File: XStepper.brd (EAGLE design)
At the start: 100.3 x 80 mm, 75 parts, among them IC2 7812TV, Q2 16 MHZ

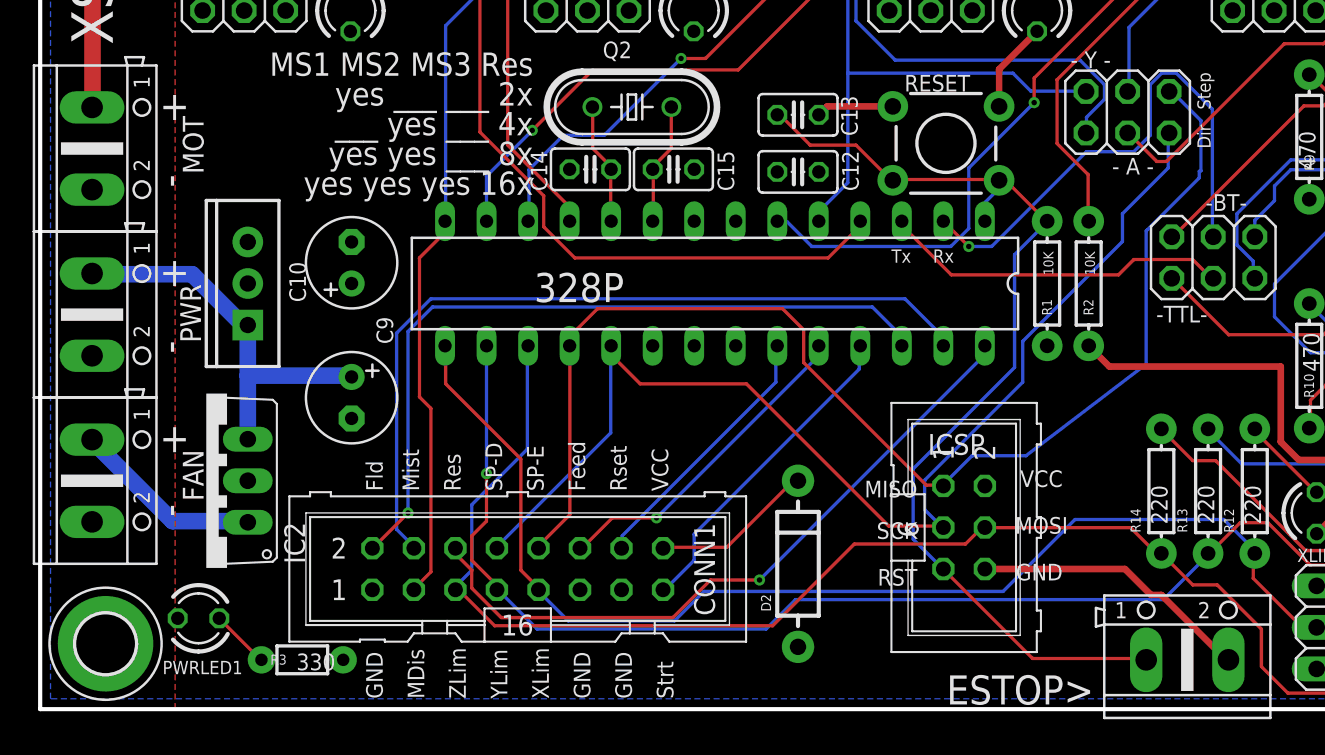
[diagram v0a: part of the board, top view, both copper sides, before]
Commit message: - add 7812 regulator for fan and main 5V voltage regulator
- change c10 to small cap cuz he get only 12v with new regulator
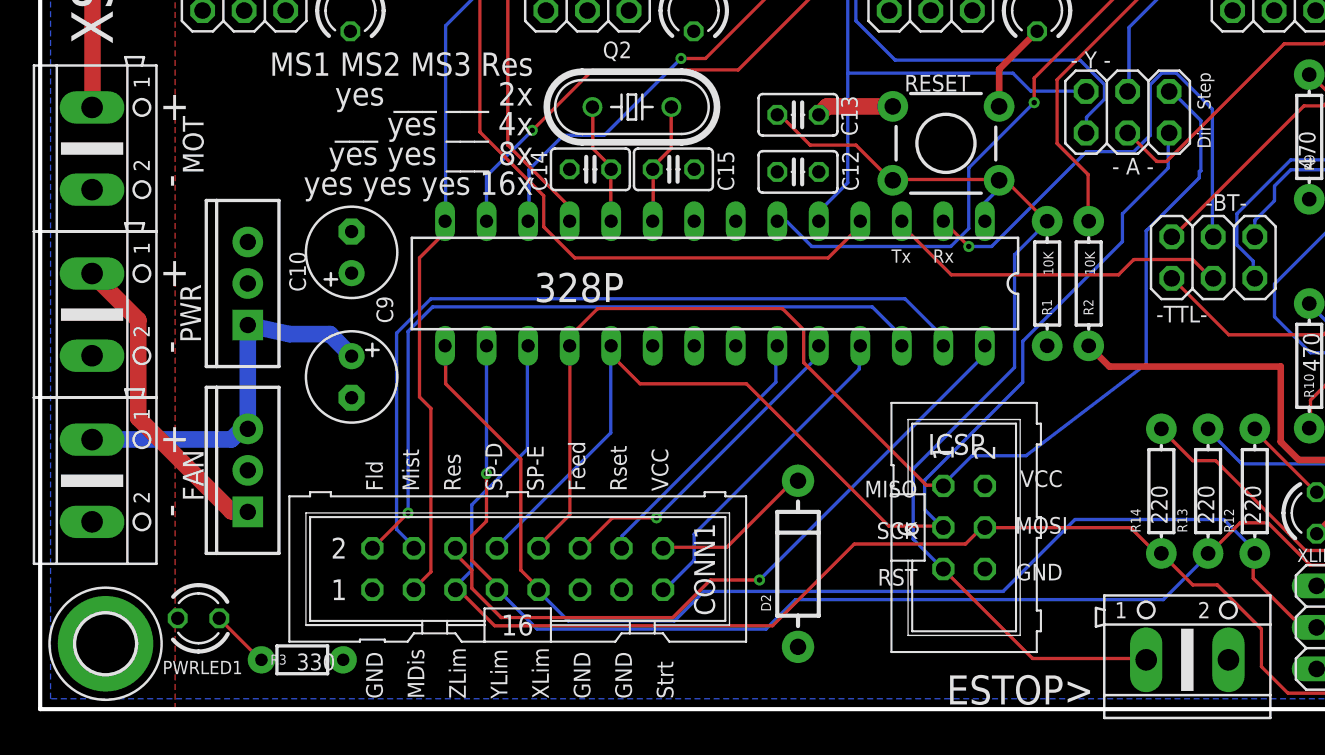
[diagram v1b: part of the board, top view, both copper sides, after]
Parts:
- removed IC2: 7812TV, linear:TO220V
- added 7812: (no value), SparkFun-PowerIC:TO220-IGO
- moved C9 1.27 mm to (19.1, 20.3)
- moved C10 0.64 mm to (19.1, 27.9)
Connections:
- removed net N$46: FAN.1, IC2.1
- new net +24V: 7812.IN, PWR.1
- net 12V: now also 7812.OUT, FAN.1; no longer IC2.3, PWR.1
- net GND: now also 7812.GND; no longer IC2.2
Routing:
- net +24V: track 0.00 -> 19.1 mm
- net GND: track 53.6 -> 36.8 mm
- net N$46: track 11.7 -> 0.00 mm
- net 12V: track 24.2 -> 23.1 mm
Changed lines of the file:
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@@
 <attribute name="VALUE" x="71.8332" y="66.087" size="1.27" layer="27" ratio="10" rot="R90"/>
 </element>
-<element name="C9" library="resistor" package="E2,5-6" value="200uF" x="19.05" y="19.05" smashed="yes" rot="R270">
-<attribute name="NAME" x="20.574" y="24.003" size="1.016" layer="25" font="vector" ratio="10" rot="R270"/>
-<attribute name="VALUE" x="22.4155" y="21.463" size="1.27" layer="27" ratio="10" rot="R270"/>
-</element>
-<element name="C10" library="resistor" package="E2,5-6" value="100uF" x="19.05" y="27.305" smashed="yes" rot="R90">
-<attribute name="NAME" x="16.256" y="24.892" size="1.016" layer="25" font="vector" ratio="10" rot="R90"/>
+<element name="C9" library="resistor" package="E2,5-6" value="200uF" x="19.05" y="20.32" smashed="yes" rot="R270">
+<attribute name="NAME" x="20.574" y="25.273" size="1.016" layer="25" font="vector" ratio="10" rot="R270"/>
+<attribute name="VALUE" x="22.4155" y="22.733" size="1.27" layer="27" ratio="10" rot="R270"/>
+</element>
+<element name="C10" library="resistor" package="E2,5-6" value="100uF" x="19.05" y="27.94" smashed="yes" rot="R90">
+<attribute name="NAME" x="16.256" y="25.527" size="1.016" layer="25" font="vector" ratio="10" rot="R90"/>
 </element>
 <element name="C12" library="resistor" package="C025-025X050" value="0.1uF" x="46.355" y="32.8613" smashed="yes" rot="R180">
@@
 </element>
 <element name="D2" library="SparkFun-DiscreteSemi" package="DIODE-1N4001" value="" x="46.355" y="8.89" rot="R90"/>
-<element name="IC2" library="linear" package="TO220V" value="7812TV" x="10.16" y="13.97" rot="R90"/>
+<element name="7812" library="SparkFun-PowerIC" package="TO220-IGO" value="" x="12.7" y="14.605" rot="R90"/>
 </elements>
 <signals>
@@
 <wire x1="58.6549" y1="36.8681" x2="58.6549" y2="39.1386" width="0.4064" layer="1"/>
 <wire x1="58.6549" y1="39.1386" x2="60.9763" y2="41.46" width="0.4064" layer="1"/>
-<wire x1="52.1525" y1="36.8681" x2="48.1394" y2="36.8681" width="0.4064" layer="1"/>
-<wire x1="48.1394" y1="36.8681" x2="47.625" y2="36.3537" width="0.4064" layer="1"/>
-<wire x1="57.785" y1="8.5725" x2="66.3575" y2="8.5725" width="0.4064" layer="1"/>
-<wire x1="66.3575" y1="8.5725" x2="67.945" y2="6.985" width="0.4064" layer="1"/>
-<wire x1="67.945" y1="6.985" x2="68.58" y2="6.985" width="0.4064" layer="1"/>
-<wire x1="68.58" y1="6.985" x2="72.39" y2="3.175" width="0.4064" layer="1"/>
+<wire x1="52.1525" y1="36.8681" x2="48.1394" y2="36.8681" width="1.016" layer="1"/>
+<wire x1="48.1394" y1="36.8681" x2="47.625" y2="36.3537" width="1.016" layer="1"/>
 <wire x1="64.135" y1="22.225" x2="65.405" y2="20.955" width="0.4064" layer="1"/>
 <wire x1="78.08" y1="10.73" x2="80.01" y2="12.7" width="0.4064" layer="1"/>
@@
 <wire x1="75.8825" y1="16.35125" x2="75.8825" y2="20.955" width="0.4064" layer="1"/>
 <wire x1="75.8825" y1="20.955" x2="65.405" y2="20.955" width="0.4064" layer="1"/>
-<contactref element="IC2" pad="2"/>
+<contactref element="7812" pad="GND"/>
 </signal>
 <signal name="N$5">
@@
 <signal name="12V" class="1">
 <contactref element="C9" pad="+"/>
-<contactref element="PWR" pad="1"/>
 <contactref element="IC1" pad="IN"/>
-<contactref element="IC2" pad="3"/>
-<wire x1="12.7" y1="23.495" x2="12.7" y2="20.4" width="1.016" layer="16"/>
-<wire x1="12.7" y1="20.4" x2="12.7" y2="16.51" width="1.016" layer="16"/>
-<wire x1="12.7" y1="20.4" x2="19" y2="20.4" width="1.016" layer="16"/>
-<wire x1="19" y1="20.4" x2="19.05" y2="20.32" width="1.016" layer="16"/>
-<wire x1="9.3" y1="26.6" x2="3.2" y2="26.6" width="1.016" layer="16"/>
-<wire x1="12.2" y1="23.7" x2="9.3" y2="26.6" width="1.016" layer="16"/>
-<wire x1="3.2" y1="26.6" x2="3.175" y2="26.6446" width="1.016" layer="16"/>
-<wire x1="12.2" y1="23.7" x2="12.7" y2="23.495" width="1.016" layer="16"/>
+<wire x1="12.7" y1="23.495" x2="15.24" y2="22.94" width="1.016" layer="16"/>
+<wire x1="15.24" y1="22.94" x2="17.73" y2="22.94" width="1.016" layer="16"/>
+<wire x1="17.73" y1="22.94" x2="19.05" y2="21.59" width="1.016" layer="16"/>
+<contactref element="7812" pad="OUT"/>
+<contactref element="FAN" pad="1"/>
+<wire x1="12.7" y1="23.495" x2="12.7" y2="17.145" width="1.016" layer="16"/>
+<wire x1="11.7" y1="16.5" x2="3.2" y2="16.5" width="1.016" layer="16"/>
+<wire x1="12.2" y1="17" x2="11.7" y2="16.5" width="1.016" layer="16"/>
+<wire x1="3.2" y1="16.5" x2="3.175" y2="16.4846" width="1.016" layer="16"/>
+<wire x1="12.2" y1="17" x2="12.7" y2="17.145" width="1.016" layer="16"/>
 </signal>
 <signal name="N$13">
@@
 <wire x1="93.8" y1="25.7" x2="93.82125" y2="26.3525" width="1.016" layer="1"/>
 </signal>
-<signal name="N$46" class="1">
-<contactref element="FAN" pad="1"/>
-<contactref element="IC2" pad="1"/>
-<wire x1="8.1" y1="11.5" x2="12.7" y2="11.5" width="1.016" layer="16"/>
-<wire x1="3.2" y1="16.4" x2="8.1" y2="11.5" width="1.016" layer="16"/>
-<wire x1="12.7" y1="11.5" x2="12.7" y2="11.43" width="1.016" layer="16"/>
-<wire x1="3.2" y1="16.4" x2="3.175" y2="16.4846" width="1.016" layer="16"/>
+<signal name="+24V" class="1">
+<contactref element="PWR" pad="1"/>
+<contactref element="7812" pad="IN"/>
+<wire x1="11.7" y1="12.1" x2="12.7" y2="12.1" width="1.016" layer="1"/>
+<wire x1="6" y1="17.8" x2="11.7" y2="12.1" width="1.016" layer="1"/>
+<wire x1="6" y1="23.8" x2="6" y2="17.8" width="1.016" layer="1"/>
+<wire x1="3.2" y1="26.6" x2="6" y2="23.8" width="1.016" layer="1"/>
+<wire x1="12.7" y1="12.1" x2="12.7" y2="12.065" width="1.016" layer="1"/>
+<wire x1="3.2" y1="26.6" x2="3.175" y2="26.6446" width="1.016" layer="1"/>
 </signal>
 </signals>
+<errors>
+</errors>
 </board>
 </drawing>

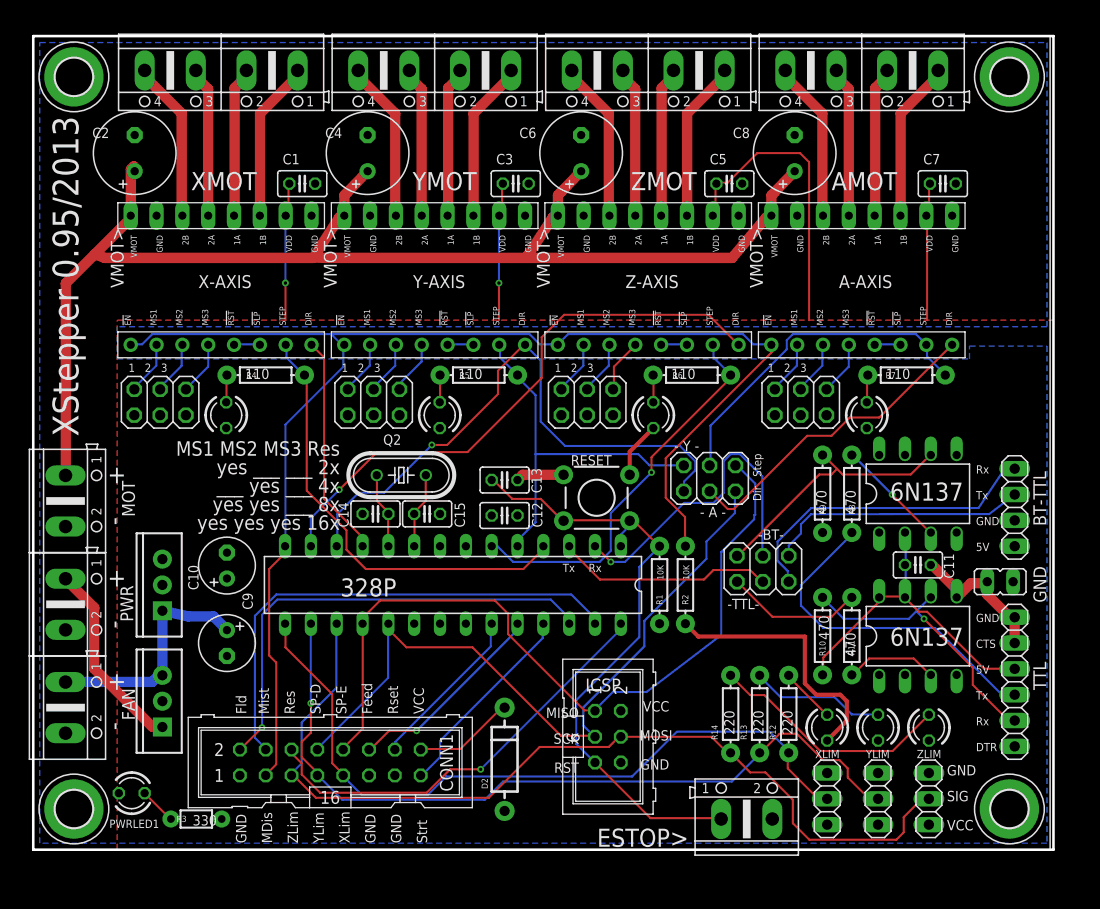
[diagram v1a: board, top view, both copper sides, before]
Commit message: - last design from matt
- correct some issues
- run all eagle tests
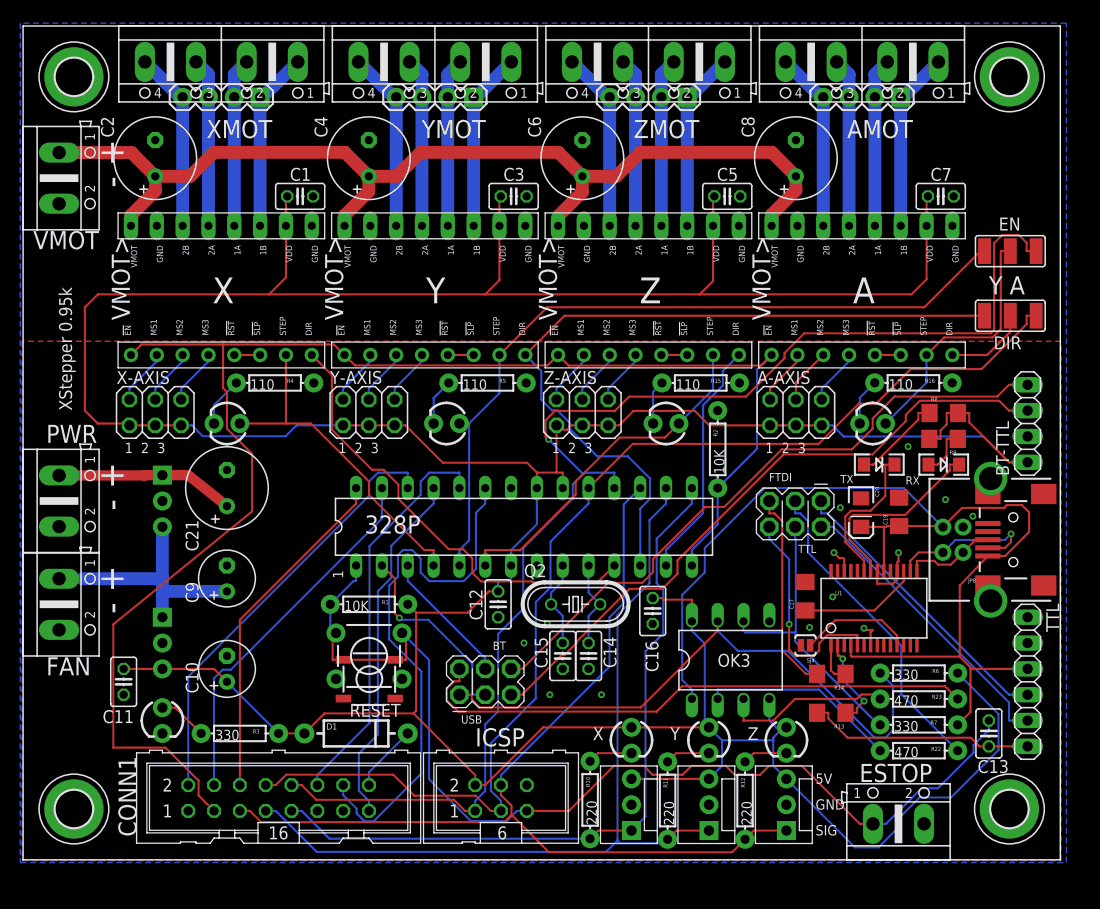
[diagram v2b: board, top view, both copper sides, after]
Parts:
- removed 7812: (no value), SparkFun-PowerIC:TO220-IGO
- removed ALED, PWRLED1, XLED, XSTLED, YLED, YSTLED, ZLED, ZSTLED: (no value), led:LED3MM
- removed COMMSEL: (no value), pinhead:2X03
- removed D2: (no value), SparkFun-DiscreteSemi:DIODE-1N4001
- removed ESTOP>, MOT: (no value), con-ptr500:AK500/2
- removed GND: (no value), jumper:JP1
- removed OK1, OK2: 6N137, optocoupler:DIL08
- added AD, XD, YD, ZD: green, SparkFun-LED:LED3MM
- added C16: 0.1uF, resistor:C025-025X050
- added C17, C19: 0.1uF, SparkFun-Capacitors:1206
- added C20: 10uF, SparkFun-Capacitors:EIA3216
- added C21: 200uF, resistor:E3,5-8
- added D1: (no value), SparkFun-DiscreteSemi:DIODE-1N4001
- added DIR: DIR, SparkFun-Passives:SJ_2W
- added EN: EN, SparkFun-Passives:SJ_2W
- added ESTOP, VMOT: (no value), con-ptr500:AK500/2
- added IC2: L7812, SparkFun-PowerIC:TO220-IGO
- added JP2, JP3, JP4: (no value), SparkFun-Connectors:1X04
- added JP5, JP6: (no value), SparkFun-Connectors:2X3_POGO
- added JP7: USBSMD, SparkFun-Connectors:USB-MINIB
- added JP8: USB-B, SparkFun-Connectors:USB-B-PTH
- added OK3: HCPL2630, optocoupler:DIL08
- added R15, R16: 110, SparkFun-Resistors:AXIAL-0.3
- added R22, R23: 470, SparkFun-Resistors:AXIAL-0.3
- added RX: Grn, SparkFun-LED:LED-1206
- added S1: (no value), SparkFun-Electromechanical:TACTILE_SWITCH_SMD
- added SJ4: NO, SparkFun-Passives:SJ_2S-NO
- added TX: Red, SparkFun-LED:LED-1206
- added U1: FT232RL-BASICSSOP, SparkFun-DigitalIC:SSOP28DB
- added VCC: orange, SparkFun-LED:LED3MM
- added X, Y, Z: red, SparkFun-LED:LED3MM
- A-AXIS, X-AXIS, Y-AXIS, Z-AXIS: value (none) -> 2x03
- C10: value 100uF -> 47uF
- C9: value 200uF -> 100uF
- IC1: value (none) -> L7805
- JP1: device pinhead:2X03 -> SparkFun-Connectors:1X04
- R10, R11: value 470 -> 220
- R13, R14: value 220 -> 10K; device SparkFun-Resistors:AXIAL-0.3 -> SparkFun-Resistors:1206
- R3: device SparkFun-Resistors:1/6W-RES -> SparkFun-Resistors:AXIAL-0.3
- R6, R7: value 110 -> 330
- R8, R9: value 470 -> 1K; device SparkFun-Resistors:AXIAL-0.3 -> SparkFun-Resistors:1206
- XLIM, YLIM, ZLIM: device pinhead:1X03 -> SparkFun-Connectors:MOLEX-1X3
- moved H5 116.8 mm to (4.00, 4.00)
- moved H8 116.8 mm to (4.00, 76.0)
- moved H6 92.0 mm to (96.0, 4.00)
- moved H7 92.0 mm to (96.0, 76.0)
- moved C11 79.0 mm to (8.89, 16.5), turned to 90 degrees
- moved JP1 58.0 mm to (22.3, 74.0)
- moved C13 53.7 mm to (94.0, 11.4), turned to 90 degrees
- moved R6 36.8 mm to (87.1, 17.4)
- moved R7 34.4 mm to (87.1, 12.3)
- moved R1 28.6 mm to (33.0, 24.1), turned to 0 degrees
- moved R10 28.0 mm to (54.8, 4.89), turned to 90 degrees
- moved RESET 27.3 mm to (33.0, 19.1), turned to 180 degrees
- moved C14 25.2 mm to (54.6, 19.1), turned to 270 degrees
- moved R11 24.3 mm to (62.4, 4.83)
- moved Q2 21.3 mm to (53.3, 24.1), turned to 0 degrees
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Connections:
- net MOTOR_DISABLE renamed ENABLE
- removed net +24V: 7812.IN, PWR.1
- removed net 12V: 7812.OUT, C9.+, FAN.1, IC1.IN
- removed net BTRXD: BT-TTL.3, COMMSEL.6
- removed net BTTXD: BT-TTL.4, COMMSEL.5
- removed net N$10: STEPPERDRIVER1.1A, YMOT.2
- removed net N$27: AMOT.3, STEPPERDRIVER3.2A
- removed net N$38: R4.P$1, XLED.A
- removed net N$39: R5.P$1, YLED.A
- removed net N$40: R6.P$1, ZLED.A
- removed net N$41: ALED.A, R7.P$1
- removed net N$42: R13.P$2, YSTLED.A
- removed net N$44: R14.P$2, ZSTLED.A
- removed net PWRMOT: C2.+, C4.+, C6.+, C8.+, MOT.1, STEPPERDRIVER.VMOT, STEPPERDRIVER1.VMOT, STEPPERDRIVER2.VMOT, STEPPERDRIVER3.VMOT
- removed net RXD: 328P.2, COMMSEL.4
- removed net RXDUSB: COMMSEL.2, OK2.6, R9.P$2
- removed net TXD: 328P.3, COMMSEL.3
- removed net TXDUSB: COMMSEL.1, R11.P$2
- removed net USB_5V: C11.1, OK1.7, OK1.8, OK2.2, R10.P$2, TTL.3
- removed net USB_GND: C11.2, GND.1, OK1.5, TTL.1, TTL.2
- removed net USB_RXD: OK1.6, R10.P$1, TTL.5
- removed net USB_TXD: R8.P$1, TTL.4
- new net +12V: C9.+, FAN.1, IC1.IN, IC2.OUT
- new net 1AA: AMOT.2, JP4.2, STEPPERDRIVER3.1A
- new net 1AX: JP1.2, STEPPERDRIVER.1A, XMOT.2
- new net 1AY: JP2.2, STEPPERDRIVER1.1A, YMOT.2
- new net 1AZ: JP3.2, STEPPERDRIVER2.1A, ZMOT.2
- new net 1BA: AMOT.1, JP4.1, STEPPERDRIVER3.1B
- new net 1BX: JP1.1, STEPPERDRIVER.1B, XMOT.1
- new net 1BY: JP2.1, STEPPERDRIVER1.1B, YMOT.1
- new net 1BZ: JP3.1, STEPPERDRIVER2.1B, ZMOT.1
- new net 2AA: AMOT.3, JP4.3, STEPPERDRIVER3.2A
- new net 2AX: JP1.3, STEPPERDRIVER.2A, XMOT.3
- new net 2AY: JP2.3, STEPPERDRIVER1.2A, YMOT.3
- new net 2AZ: JP3.3, STEPPERDRIVER2.2A, ZMOT.3
- new net 2BA: AMOT.4, JP4.4, STEPPERDRIVER3.2B
- new net 2BX: JP1.4, STEPPERDRIVER.2B, XMOT.4
- new net 2BY: JP2.4, STEPPERDRIVER1.2B, YMOT.4
- new net 2BZ: JP3.4, STEPPERDRIVER2.2B, ZMOT.4
- new net BT_RXD: BT-TTL.4, JP5.P$6
- new net BT_TXD: BT-TTL.3, JP5.P$5
- new net DTR: C13.1, R13.2, TTL.6
- new net FTDI_RX: JP6.P$6, U1.5
- new net FTDI_TX: JP6.P$5, R14.2
- new net N$46: OK3.3, R23.P$2
- new net N$47: OK3.2, R22.P$2
- new net OPTO_RX: JP6.P$4, OK3.6, R7.P$1
- new net OPTO_TX: JP6.P$3, R22.P$1
- new net RX: 328P.2, JP5.P$3
- new net RXD_USB: JP5.P$2, R23.P$1
- new net TTL/USB_5V: C19.1, C20.A, JP7.VBUS, JP8.VBUS, OK3.1, R7.P$2, TTL.3, U1.20, U1.4
- new net TTL_RX: JP6.P$2, TTL.5
- new net TTL_TX: JP6.P$1, TTL.4
- new net TX: 328P.3, JP5.P$4
- new net TXD_USB: JP5.P$1, OK3.7, R6.P$1
- new net VIN: C21.+, IC2.IN, PWR.1
- new net VMOT: C2.+, C4.+, C6.+, C8.+, STEPPERDRIVER.VMOT, STEPPERDRIVER1.VMOT, STEPPERDRIVER2.VMOT, STEPPERDRIVER3.VMOT, VMOT.1
- net 5V: now also C1.1, C11.2, C16.2, C3.1, C5.1, C7.1, D1.A, OK3.4, OK3.8, R3.P$2, R6.P$2, R8.2, R9.2, X.A, XLIM.3, Y.A, YLIM.3, Z.A, ZLIM.3; no longer C1.2, C3.2, C5.2, C7.2, D2.A, OK1.2, OK2.7, OK2.8, R3.1, R9.P$1, XLIM.1, YLIM.1, ZLIM.1
- net A-DIR: now also DIR.2; no longer JP1.4
- net A-STEP: now also AD.A, EN.2; no longer JP1.3, R7.P$2
- net GND: now also C1.2, C11.1, C16.1, C17.2, C19.2, C20.C, C21.-, C3.2, C5.2, C7.2, ESTOP.2, IC2.GND, JP7.GND, JP8.GND, OK3.5, R15.P$2, R16.P$2, R4.P$2, R5.P$2, S1.1, S1.2, SJ4.2, TTL.1, U1.18, U1.21, U1.25, U1.26, U1.7, VCC.K, VMOT.2, XLIM.2, YLIM.2, ZLIM.2; no longer 7812.GND, ALED.K, C1.1, C13.1, C3.1, C5.1, C7.1, ESTOP>.2, GND.2, MOT.2, OK2.5, PWRLED1.K, XLED.K, XLIM.3, XSTLED.K, YLED.K, YLIM.3, YSTLED.K, ZLED.K, ZLIM.3, ZSTLED.K
- net N$1: now also C17.1, U1.17; no longer STEPPERDRIVER.1B, XMOT.1
- net N$11: now also TX.C, U1.23; no longer STEPPERDRIVER1.2A, YMOT.3
- net N$12: now also RX.C, U1.22; no longer STEPPERDRIVER1.2B, YMOT.4
- net N$17: now also R9.1, RX.A; no longer STEPPERDRIVER2.2B, ZMOT.4
- net N$18: now also R8.1, TX.A; no longer STEPPERDRIVER2.2A, ZMOT.3
- net N$19: now also SJ4.1, U1.11; no longer STEPPERDRIVER2.1A, ZMOT.2
- net N$2: now also JP7.D+, JP8.D+, U1.15; no longer STEPPERDRIVER.1A, XMOT.2
- net N$20: now also R4.P$1, XD.K; no longer STEPPERDRIVER2.1B, ZMOT.1
- net N$25: now also R5.P$1, YD.K; no longer AMOT.1, STEPPERDRIVER3.1B
- net N$26: now also R15.P$1, ZD.K; no longer AMOT.2, STEPPERDRIVER3.1A
- net N$28: now also AD.K, R16.P$1; no longer AMOT.4, STEPPERDRIVER3.2B
- net N$3: now also JP7.D-, JP8.D-, U1.16; no longer STEPPERDRIVER.2A, XMOT.3
- net N$35: now also R10.P$2, X.K; no longer OK2.3, R8.P$2
- net N$36: now also R11.P$2, Y.K; no longer OK1.3, R11.P$1
- net N$37: now also Z.K; no longer XSTLED.A
- net N$4: now also R13.1, U1.2; no longer STEPPERDRIVER.2B, XMOT.4
- net N$43: now also R3.P$1, VCC.A; no longer PWRLED1.A, R3.2
- net N$45: now also D1.C; no longer D2.C
- net N$9: now also R14.1, U1.1; no longer STEPPERDRIVER1.1B, YMOT.1
- net RESET: now also ESTOP.1, S1.3, S1.4; no longer ESTOP>.1
- net SPINDLE-DIR: now also DIR.3; no longer JP1.2
- net SPINDLE-ENABLE: now also EN.1; no longer JP1.1
- net X-STEP: now also XD.A; no longer R4.P$2
- net X-STOP: now also R10.P$1, XLIM.1; no longer R12.P$1, XLIM.2
- net Y-DIR: now also DIR.1; no longer JP1.6
- net Y-STEP: now also EN.3, YD.A; no longer JP1.5, R5.P$2
- net Y-STOP: now also R11.P$1, YLIM.1; no longer R13.P$1, YLIM.2
- net Z-STEP: now also ZD.A; no longer R6.P$2
- net Z-STOP: now also R12.P$1, ZLIM.1; no longer R14.P$1, ZLIM.2
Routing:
- net 5V: track 70.6 -> 437.5 mm, vias 2 -> 0
- net PWRMOT: track 129.0 -> 0.00 mm
- net TTL/USB_5V: track 0.00 -> 108.7 mm
- net VMOT: track 0.00 -> 102.7 mm
- net BT_TXD: track 0.00 -> 64.5 mm
- net BT_RXD: track 0.00 -> 63.8 mm
- net TXD_USB: track 0.00 -> 59.2 mm
- net RXD_USB: track 0.00 -> 56.1 mm
- net SPINDLE-ENABLE: track 77.2 -> 130.3 mm, vias 0 -> 1
- net RESET: track 62.3 -> 104.3 mm
- net SPINDLE-DIR: track 71.4 -> 112.7 mm
- net Y-STEP: track 37.1 -> 75.2 mm
- net G-RESET: track 16.4 -> 53.9 mm
- net USB_TXD: track 33.9 -> 0.00 mm
- net USB_5V: track 33.5 -> 0.00 mm
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- added copper zone on layer 1, net GND
- removed copper zone on layer 1, net 5V
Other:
- board size 100.3 x 80 mm -> 102 x 82 mm
- board text added: "- +"
- board text added: "1"
- board text added: "A"
- board text added: "BT"
- board text added: "FTDI"
- board text added: "TTL"
- board text added: "USB"
- board text added: "X"
- board text added: "XStepper 0.95k"
- board text added: "Y"
- board text added: "Y A"
- board text added: "Z"
- board text removed: "+"
- board text removed: "-"
- board text removed: "- A -"
- board text removed: "- Y -"
- board text removed: "-BT-"
- board text removed: "-TTL-"
- board text removed: "6N137"
- board text removed: "C6"
- board text removed: "C8"
- board text removed: "CTS"
- board text removed: "DTR"
- board text removed: "Dir"
- board text removed: "Feed"
- board text removed: "Fld"
- board text removed: "MDis"
- board text removed: "MISO"
- board text removed: "MOSI"
- board text removed: "MS1 MS2 MS3 Res yes ___ ___ 2x ___ yes ___ 4x yes yes ___ 8x yes yes yes 16x"
- board text removed: "Mist"
- board text removed: "RST"
- board text removed: "Res"
- board text removed: "Rset"
- board text removed: "Rx"
- board text removed: "SCK"
- board text removed: "SP-D"
- board text removed: "SP-E"
- board text removed: "Step"
- board text removed: "Strt"
- board text removed: "Tx"
- board text removed: "VCC"
- board text removed: "XLim"
- board text removed: "XStepper 0.95/2013"
- board text removed: "YLim"
- board text removed: "ZLim"
